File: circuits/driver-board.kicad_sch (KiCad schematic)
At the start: 74 parts, among them J1 Conn_01x18_Female, J2 USB4120-03-C_REVA, J3 Motor_Conn_01x04, J4 Screw_Terminals, J5 Conn_01x06_Female, Q1 SS8050-G, Q2 SS8050-G, SW1 RST_SW_Push, U1 CP2102N-Axx-xQFN24, U2 BA33DD0T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

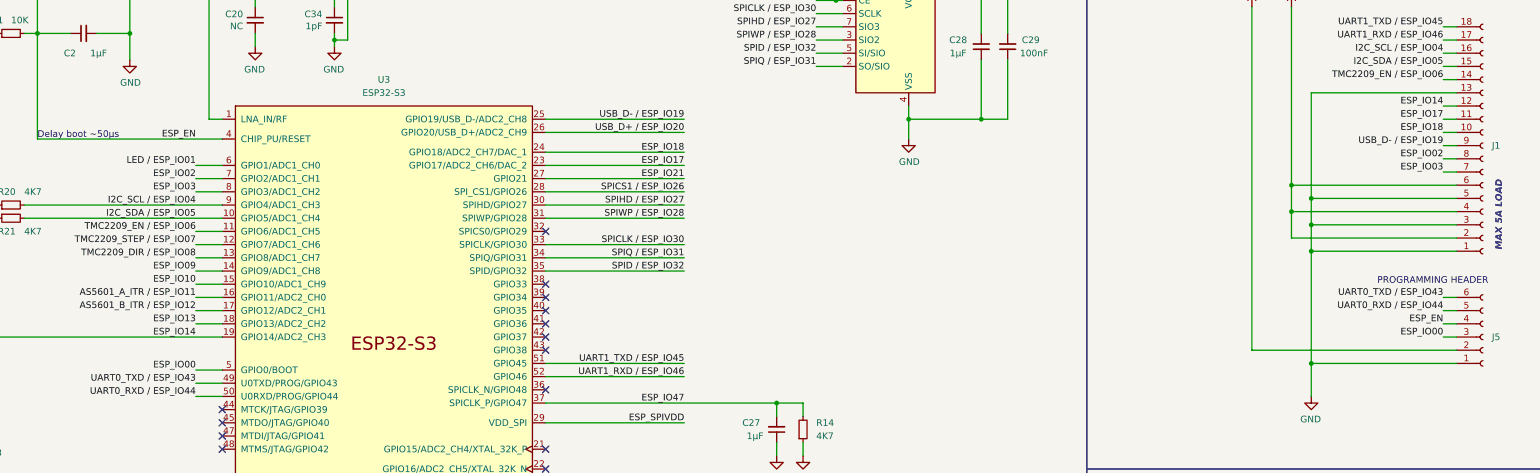
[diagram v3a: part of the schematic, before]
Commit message: another round of overall placement
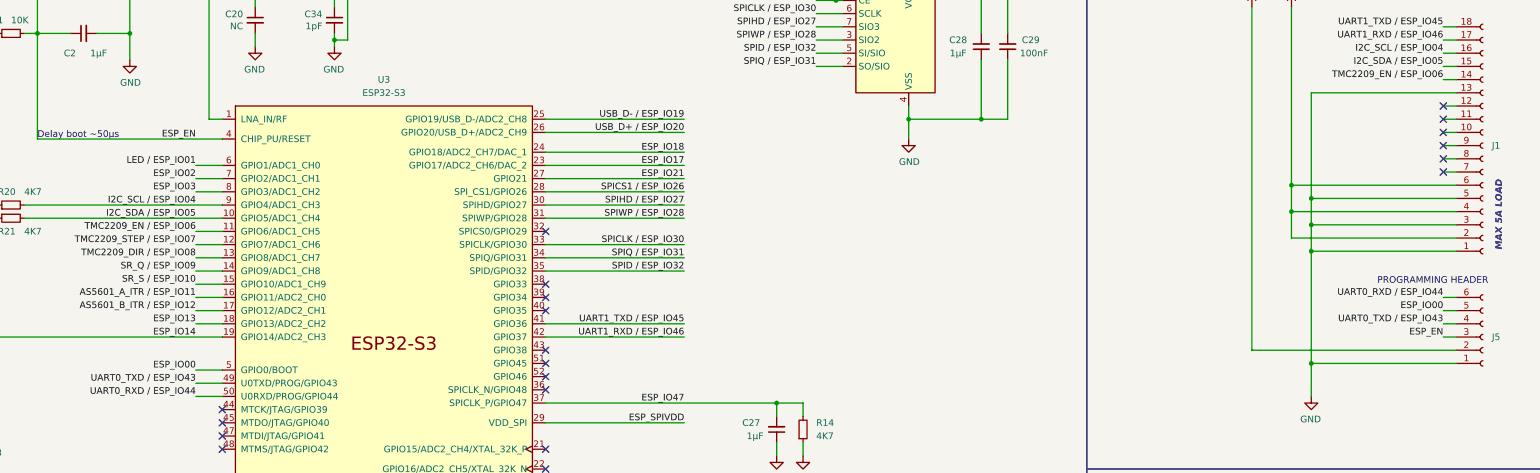
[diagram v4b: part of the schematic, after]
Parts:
- U8: footprint Package_SON:X2SON-8_1.4x1mm_P0.35mm -> Package_SO:TSSOP-8_3x3mm_P0.65mm
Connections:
- net ESP_IO09 is gone; now on net SR_Q / ESP_IO09: U3.14 (GPIO9/ADC1_CH8)
- net ESP_IO10 is gone; now on net SR_S / ESP_IO10: U3.15 (GPIO10/ADC1_CH9)
- net ESP_EN: now also J5.3 (Pin_3); no longer J5.4 (Pin_4)
- net ESP_IO00: now also J5.5 (Pin_5); no longer J5.3 (Pin_3)
- net ESP_IO02: no longer J1.8 (Pin_8)
- net ESP_IO03: no longer J1.7 (Pin_7)
- net ESP_IO14: no longer J1.12 (Pin_12)
- net ESP_IO17: no longer J1.11 (Pin_11)
- net ESP_IO18: no longer J1.10 (Pin_10)
- net UART0_RXD / ESP_IO44: now also J5.6 (Pin_6); no longer J5.5 (Pin_5)
- net UART0_TXD / ESP_IO43: now also J5.4 (Pin_4); no longer J5.6 (Pin_6)
- net UART1_RXD / ESP_IO46: now also U3.42 (GPIO37); no longer U3.52 (GPIO46)
- net UART1_TXD / ESP_IO45: now also U3.41 (GPIO36); no longer U3.51 (GPIO45)
- net USB_D- / ESP_IO19: no longer J1.9 (Pin_9)
- no-connect marks 48 -> 54
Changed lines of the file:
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@@
   (no_connect (at 69.85 63.5))
   (no_connect (at 64.77 246.38))
+  (no_connect (at 302.26 243.84))
   (no_connect (at 240.03 257.81))
   (no_connect (at 85.09 157.48))
+  (no_connect (at 474.98 199.39))
   (no_connect (at 240.03 252.73))
   (no_connect (at 54.61 157.48))
@@
   (no_connect (at 64.77 259.08))
   (no_connect (at 85.09 170.18))
+  (no_connect (at 474.98 196.85))
+  (no_connect (at 302.26 246.38))
   (no_connect (at 474.98 116.84))
   (no_connect (at 227.33 114.3))
@@
   (no_connect (at 74.93 132.08))
   (no_connect (at 227.33 68.58))
+  (no_connect (at 474.98 207.01))
   (no_connect (at 240.03 255.27))
-  (no_connect (at 302.26 238.76))
   (no_connect (at 227.33 71.12))
   (no_connect (at 54.61 172.72))
   (no_connect (at 64.77 264.16))
+  (no_connect (at 474.98 194.31))
+  (no_connect (at 474.98 201.93))
   (no_connect (at 302.26 231.14))
   (no_connect (at 302.26 233.68))
   (no_connect (at 64.77 256.54))
+  (no_connect (at 474.98 204.47))
   (no_connect (at 85.09 167.64))
-  (no_connect (at 302.26 236.22))
   (no_connect (at 240.03 260.35))
   (no_connect (at 302.26 248.92))
@@
     (stroke (width 0) (type default) (color 0 0 0 0))
   )
-  (wire (pts (xy 302.26 243.84) (xy 328.93 243.84))
+  (wire (pts (xy 302.26 236.22) (xy 328.93 236.22))
     (stroke (width 0) (type default) (color 0 0 0 0))
   )
@@
     (stroke (width 0) (type default) (color 0 0 0 0))
   )
-  (wire (pts (xy 302.26 246.38) (xy 328.93 246.38))
+  (wire (pts (xy 302.26 238.76) (xy 328.93 238.76))
     (stroke (width 0) (type default) (color 0 0 0 0))
   )
@@
     (effects (font (size 1.27 1.27)) (justify right bottom))
   )
-  (label "UART0_RXD {slash} ESP_IO44" (at 474.98 233.68 180)
+  (label "UART0_RXD {slash} ESP_IO44" (at 474.98 231.14 180)
     (effects (font (size 1.27 1.27)) (justify right bottom))
   )
@@
     (effects (font (size 1.27 1.27)) (justify right bottom))
   )
-  (label "ESP_IO00" (at 474.98 238.76 180)
+  (label "ESP_IO00" (at 474.98 233.68 180)
     (effects (font (size 1.27 1.27)) (justify right bottom))
   )
@@
     (effects (font (size 1.27 1.27)) (justify right bottom))
   )
-  (label "ESP_IO10" (at 234.95 228.6 180)
-    (effects (font (size 1.27 1.27)) (justify right bottom))
-  )
   (label "TMC2209_DIAG" (at 222.25 101.6 180)
     (effects (font (size 1.27 1.27)) (justify right bottom))
@@
     (effects (font (size 1.27 1.27)) (justify right bottom))
   )
-  (label "ESP_IO03" (at 474.98 207.01 180)
-    (effects (font (size 1.27 1.27)) (justify right bottom))
-  )
   (label "TMC2209_OB2" (at 281.94 95.25 180)
     (effects (font (size 1.27 1.27)) (justify right bottom))
@@
     (effects (font (size 1.27 1.27)) (justify right bottom))
   )
-  (label "UART1_RXD {slash} ESP_IO46" (at 328.93 246.38 180)
+  (label "UART1_RXD {slash} ESP_IO46" (at 328.93 238.76 180)
     (effects (font (size 1.27 1.27)) (justify right bottom))
   )
@@
     (effects (font (size 1.27 1.27)) (justify right bottom))
   )
-  (label "ESP_IO09" (at 234.95 226.06 180)
-    (effects (font (size 1.27 1.27)) (justify right bottom))
-  )
   (label "LED {slash} ESP_IO01" (at 234.95 205.74 180)
     (effects (font (size 1.27 1.27)) (justify right bottom))
@@
     (effects (font (size 1.27 1.27)) (justify right bottom))
   )
-  (label "UART0_TXD {slash} ESP_IO43" (at 474.98 231.14 180)
+  (label "UART0_TXD {slash} ESP_IO43" (at 474.98 236.22 180)
     (effects (font (size 1.27 1.27)) (justify right bottom))
   )
@@
     (effects (font (size 1.27 1.27)) (justify right bottom))
   )
+  (label "SR_Q {slash} ESP_IO09" (at 234.95 226.06 180)
+    (effects (font (size 1.27 1.27)) (justify right bottom))
+  )
   (label "ESP_IO21" (at 328.93 208.28 180)
     (effects (font (size 1.27 1.27)) (justify right bottom))
@@
     (effects (font (size 1.27 1.27)) (justify right bottom))
   )
-  (label "ESP_EN" (at 474.98 236.22 180)
+  (label "ESP_EN" (at 474.98 238.76 180)
     (effects (font (size 1.27 1.27)) (justify right bottom))
   )
@@
     (effects (font (size 1.27 1.27)) (justify left bottom))
   )
-  (label "ESP_IO17" (at 474.98 196.85 180)
-    (effects (font (size 1.27 1.27)) (justify right bottom))
-  )
   (label "ESP_IO14" (at 234.95 238.76 180)
     (effects (font (size 1.27 1.27)) (justify right bottom))
@@
     (effects (font (size 1.27 1.27)) (justify left bottom))
   )
-  (label "SPIWP {slash} ESP_IO28" (at 328.93 215.9 180)
+  (label "SR_S {slash} ESP_IO10" (at 234.95 228.6 180)
     (effects (font (size 1.27 1.27)) (justify right bottom))
   )
-  (label "ESP_IO14" (at 474.98 194.31 180)
+  (label "SPIWP {slash} ESP_IO28" (at 328.93 215.9 180)
     (effects (font (size 1.27 1.27)) (justify right bottom))
   )
@@
     (effects (font (size 1.27 1.27)) (justify right bottom))
   )
-  (label "ESP_IO18" (at 474.98 199.39 180)
-    (effects (font (size 1.27 1.27)) (justify right bottom))
-  )
   (label "UART1_RXD {slash} ESP_IO46" (at 474.98 181.61 180)
     (effects (font (size 1.27 1.27)) (justify right bottom))
@@
     (effects (font (size 1.27 1.27)) (justify right bottom))
   )
-  (label "USB_D- {slash} ESP_IO19" (at 474.98 201.93 180)
-    (effects (font (size 1.27 1.27)) (justify right bottom))
-  )
   (label "USB_D+" (at 107.95 60.96 0)
     (effects (font (size 1.27 1.27)) (justify left bottom))
@@
     (effects (font (size 1.27 1.27)) (justify right bottom))
   )
-  (label "ESP_IO02" (at 474.98 204.47 180)
-    (effects (font (size 1.27 1.27)) (justify right bottom))
-  )
   (label "UART1_TXD {slash} ESP_IO45" (at 207.01 73.66 180)
     (effects (font (size 1.27 1.27)) (justify right bottom))
   )
-  (label "UART1_TXD {slash} ESP_IO45" (at 328.93 243.84 180)
+  (label "UART1_TXD {slash} ESP_IO45" (at 328.93 236.22 180)
     (effects (font (size 1.27 1.27)) (justify right bottom))
   )
@@
       (effects (font (size 1.27 1.27)) hide)
     )
-    (property "Footprint" "Package_SON:X2SON-8_1.4x1mm_P0.35mm" (id 2) (at 372.11 129.54 0)
+    (property "Footprint" "Package_SO:TSSOP-8_3x3mm_P0.65mm" (id 2) (at 372.11 129.54 0)
       (effects (font (size 1.27 1.27)) hide)
     )
@@
     (property "Reference" "U8" (id 0) (at 373.38 114.3 0))
     (property "Value" "74LVC2G00" (id 1) (at 363.22 110.49 0))
-    (property "Footprint" "Package_SON:X2SON-8_1.4x1mm_P0.35mm" (id 2) (at 372.11 114.3 0)
+    (property "Footprint" "Package_SO:TSSOP-8_3x3mm_P0.65mm" (id 2) (at 372.11 114.3 0)
       (effects (font (size 1.27 1.27)) hide)
     )
@@
     )
     (path "/556ac974-9db3-4485-862d-ab386d9379e5"
-      (reference "U8") (unit 1) (value "74LVC2G00") (footprint "Package_SON:X2SON-8_1.4x1mm_P0.35mm")
+      (reference "U8") (unit 1) (value "74LVC2G00") (footprint "Package_SO:TSSOP-8_3x3mm_P0.65mm")
     )
     (path "/248c1e11-ccfb-48a8-8f7d-9b8a22293b8c"
-      (reference "U8") (unit 2) (value "74LVC2G00") (footprint "Package_SON:X2SON-8_1.4x1mm_P0.35mm")
+      (reference "U8") (unit 2) (value "74LVC2G00") (footprint "Package_SO:TSSOP-8_3x3mm_P0.65mm")
     )
     (path "/2eabefb1-a485-4f8d-a57b-22102eead219"

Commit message: first tracing
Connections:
- net I2C_SCL / ESP_IO04: now also J1.15 (Pin_15); no longer J1.16 (Pin_16)
- net I2C_SDA / ESP_IO05: now also J1.16 (Pin_16); no longer J1.15 (Pin_15)
- net TMC2209_STEP / ESP_IO15: now reaches U3.21 (GPIO15/ADC2_CH4/XTAL_32K_P)
- net TMC2209_STEP / ESP_IO15: now also U5.16 (STEP)
- net TMC2209_DIR / ESP_IO16: now reaches U3.22 (GPIO16/ADC2_CH5/XTAL_32K_N)
- net TMC2209_DIR / ESP_IO16: now also U5.19 (DIR)
- net ESP_IO18 renamed SR_Q / ESP_IO18
- net SR_Q / ESP_IO18: now also U8.5, U8.7
- net ESP_IO21 renamed SR_S / ESP_IO21
- net SR_S / ESP_IO21: now also R18.1, R2.2, U8.6
- removed net SR_Q / ESP_IO09: U3.14 (GPIO9/ADC1_CH8), U8.5, U8.7
- removed net SR_S / ESP_IO10: R18.1, R2.2, U3.15 (GPIO10/ADC1_CH9), U8.6
- net TMC2209_DIR / ESP_IO08: no longer names the net of U3.13 (GPIO8/ADC1_CH7)
- net TMC2209_DIR / ESP_IO08: no longer U5.19 (DIR)
- net TMC2209_STEP / ESP_IO07: no longer names the net of U3.12 (GPIO7/ADC1_CH6)
- net TMC2209_STEP / ESP_IO07: no longer U5.16 (STEP)
- new net ESP_IO09: U3.14 (GPIO9/ADC1_CH8)
- new net ESP_IO10: U3.15 (GPIO10/ADC1_CH9)
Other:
- moved on the sheet: J2, R5, R6

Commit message: first finished tracing; missing expboard connections and bom
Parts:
- removed R2: 20K, Resistor_SMD:R_0402_1005Metric, symbol Device:R_Small
- added C17: 100nF, Capacitor_SMD:C_0402_1005Metric, symbol Device:C_Small
- C5: value 1µF -> 10µF
- C7: value 10nF -> 1µF
- R20, R21: footprint Resistor_SMD:R_0201_0603Metric -> Resistor_SMD:R_0402_1005Metric
- R7: footprint Resistor_SMD:R_0402_1005Metric -> Resistor_SMD:R_0201_0603Metric
- U5: footprint Package_DFN_QFN:QFN-28-1EP_5x5mm_P0.5mm_EP3.35x3.35mm_ThermalVias -> trinamic-footprints:QFN28P
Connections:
- net ESP_IO09 is gone; now on net AS5601_A_ITR / ESP_IO09: U3.14 (GPIO9/ADC1_CH8)
- net ESP_IO10 is gone; now on net AS5601_B_ITR / ESP_IO10: U3.15 (GPIO10/ADC1_CH9)
- net +3V3: now also C17.2
- net GND: now also C17.1
- net I2C_SCL / ESP_IO04: now also J1.17 (Pin_17); no longer J1.15 (Pin_15)
- net I2C_SDA / ESP_IO05: now also J1.18 (Pin_18); no longer J1.16 (Pin_16)
- net TMC2209_EN / ESP_IO06: now also J1.16 (Pin_16); no longer J1.14 (Pin_14)
- net UART1_RXD / ESP_IO46: no longer J1.17 (Pin_17)
- net UART1_TXD / ESP_IO45: no longer J1.18 (Pin_18)
- net TMC2209_BRB: now reaches R13.2, U5.27 (BRB)
- net TMC2209_BRA: now reaches R12.2, U5.23 (BRA)
- net ANTENNA: now reaches AE1.1 (A), C34.1, L1.1
- net AS5601_A_ITR / ESP_IO11 renamed AS5601_A_ITR / ESP_IO09
- net AS5601_A_ITR / ESP_IO09: no longer U3.16 (GPIO11/ADC2_CH0)
- net AS5601_B_ITR / ESP_IO12 renamed AS5601_B_ITR / ESP_IO10
- net AS5601_B_ITR / ESP_IO10: no longer U3.17 (GPIO12/ADC2_CH1)
- net ESP_IO14 renamed VBUS_SENSE / ESP_IO14
- net LED / ESP_IO01 renamed ESP_IO01
- net ESP_IO01: no longer R4.1
- new net ESP_IO12: U3.17 (GPIO12/ADC2_CH1)
- new net LED / ESP_IO11: R4.1, U3.16 (GPIO11/ADC2_CH0)
- no-connect marks 54 -> 56
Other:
- note removed: "PULL TO BE DETERMINED"
- moved on the sheet: AE1, C25, C30, C31, C32, C33, C34, J3, R12, R13, R18

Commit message: updated groundplanes
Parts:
- removed R10, R8: 5K1, Resistor_SMD:R_0402_1005Metric, symbol Device:R_Small
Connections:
- net GND: now also J1.15 (Pin_15); no longer J1.13 (Pin_13)
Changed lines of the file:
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@@
   (junction (at 326.39 57.15) (diameter 0) (color 0 0 0 0)
   )
-  (junction (at 50.8 142.24) (diameter 0) (color 0 0 0 0)
-  )
   (junction (at 340.36 276.86) (diameter 0) (color 0 0 0 0)
   )
+  (junction (at 50.8 149.86) (diameter 0) (color 0 0 0 0)
+  )
   (junction (at 265.43 57.15) (diameter 0) (color 0 0 0 0)
   )
@@
   (junction (at 236.22 279.4) (diameter 0) (color 0 0 0 0)
   )
+  (junction (at 50.8 142.24) (diameter 0) (color 0 0 0 0)
+  )
   (junction (at 467.36 106.68) (diameter 0) (color 0 0 0 0)
   )
@@
   (junction (at 327.66 269.24) (diameter 0) (color 0 0 0 0)
   )
-  (junction (at 50.8 149.86) (diameter 0) (color 0 0 0 0)
-  )
   (junction (at 316.23 57.15) (diameter 0) (color 0 0 0 0)
   )
@@
   (junction (at 275.59 181.61) (diameter 0) (color 0 0 0 0)
   )
-  (junction (at 26.67 149.86) (diameter 0) (color 0 0 0 0)
-  )
   (junction (at 331.47 57.15) (diameter 0) (color 0 0 0 0)
   )
@@
   (no_connect (at 64.77 246.38))
   (no_connect (at 302.26 243.84))
+  (no_connect (at 474.98 191.77))
   (no_connect (at 240.03 257.81))
   (no_connect (at 85.09 157.48))
@@
   (no_connect (at 64.77 259.08))
   (no_connect (at 85.09 170.18))
-  (no_connect (at 474.98 186.69))
   (no_connect (at 474.98 196.85))
   (no_connect (at 302.26 246.38))
@@
     (stroke (width 0) (type default) (color 0 0 0 0))
   )
-  (wire (pts (xy 26.67 154.94) (xy 26.67 149.86))
-    (stroke (width 0) (type default) (color 0 0 0 0))
-  )
   (wire (pts (xy 467.36 106.68) (xy 467.36 109.22))
     (stroke (width 0) (type default) (color 0 0 0 0))
@@
     (stroke (width 0) (type default) (color 0 0 0 0))
   )
-  (wire (pts (xy 26.67 142.24) (xy 26.67 149.86))
-    (stroke (width 0) (type default) (color 0 0 0 0))
-  )
   (wire (pts (xy 354.33 173.99) (xy 358.14 173.99))
     (stroke (width 0) (type default) (color 0 0 0 0))
@@
     (stroke (width 0) (type default) (color 0 0 0 0))
   )
+  (wire (pts (xy 46.99 149.86) (xy 50.8 149.86))
+    (stroke (width 0) (type default) (color 0 0 0 0))
+  )
   (wire (pts (xy 199.39 93.98) (xy 214.63 93.98))
     (stroke (width 0) (type default) (color 0 0 0 0))
@@
     (stroke (width 0) (type default) (color 0 0 0 0))
   )
-  (wire (pts (xy 26.67 149.86) (xy 31.75 149.86))
-    (stroke (width 0) (type default) (color 0 0 0 0))
-  )
   (wire (pts (xy 386.08 162.56) (xy 391.16 162.56))
     (stroke (width 0) (type default) (color 0 0 0 0))
@@
     (stroke (width 0) (type default) (color 0 0 0 0))
   )
-  (wire (pts (xy 449.58 191.77) (xy 449.58 212.09))
+  (wire (pts (xy 449.58 186.69) (xy 449.58 212.09))
     (stroke (width 0) (type default) (color 0 0 0 0))
   )
@@
     (stroke (width 0) (type default) (color 0 0 0 0))
   )
-  (wire (pts (xy 36.83 149.86) (xy 50.8 149.86))
-    (stroke (width 0) (type default) (color 0 0 0 0))
-  )
   (wire (pts (xy 275.59 181.61) (xy 275.59 182.88))
     (stroke (width 0) (type default) (color 0 0 0 0))
@@
     (stroke (width 0) (type default) (color 0 0 0 0))
   )
+  (wire (pts (xy 46.99 142.24) (xy 50.8 142.24))
+    (stroke (width 0) (type default) (color 0 0 0 0))
+  )
   (wire (pts (xy 234.95 208.28) (xy 240.03 208.28))
     (stroke (width 0) (type default) (color 0 0 0 0))
@@
     (stroke (width 0) (type default) (color 0 0 0 0))
   )
-  (wire (pts (xy 31.75 142.24) (xy 26.67 142.24))
-    (stroke (width 0) (type default) (color 0 0 0 0))
-  )
   (wire (pts (xy 25.4 88.9) (xy 25.4 93.98))
     (stroke (width 0) (type default) (color 0 0 0 0))
@@
     (stroke (width 0) (type default) (color 0 0 0 0))
   )
-  (wire (pts (xy 474.98 186.69) (xy 477.52 186.69))
+  (wire (pts (xy 449.58 186.69) (xy 477.52 186.69))
     (stroke (width 0) (type default) (color 0 0 0 0))
   )
@@
     (stroke (width 0) (type default) (color 0 0 0 0))
   )
-  (wire (pts (xy 449.58 191.77) (xy 477.52 191.77))
-    (stroke (width 0) (type default) (color 0 0 0 0))
-  )
   (wire (pts (xy 316.23 57.15) (xy 316.23 59.69))
     (stroke (width 0) (type default) (color 0 0 0 0))
@@
     (stroke (width 0) (type default) (color 0 0 0 0))
   )
-  (wire (pts (xy 36.83 142.24) (xy 50.8 142.24))
-    (stroke (width 0) (type default) (color 0 0 0 0))
-  )
   (wire (pts (xy 379.73 113.03) (xy 383.54 113.03))
     (stroke (width 0) (type default) (color 0 0 0 0))
@@
     (stroke (width 0) (type default) (color 0 0 0 0))
   )
+  (wire (pts (xy 474.98 191.77) (xy 477.52 191.77))
+    (stroke (width 0) (type default) (color 0 0 0 0))
+  )
   (wire (pts (xy 121.92 78.74) (xy 121.92 82.55))
     (stroke (width 0) (type default) (color 0 0 0 0))
@@
     (effects (font (size 1.27 1.27)) (justify right bottom))
   )
-  (label "USB_CC1" (at 49.53 142.24 180)
+  (label "USB_CC1" (at 46.99 142.24 180)
     (effects (font (size 1.27 1.27)) (justify right bottom))
   )
@@
     (effects (font (size 1.27 1.27)) (justify left bottom))
   )
-  (label "USB_CC2" (at 49.53 149.86 180)
+  (label "USB_CC2" (at 46.99 149.86 180)
     (effects (font (size 1.27 1.27)) (justify right bottom))
   )
@@
     (pin "9")
   )
-  (symbol (lib_id "power:GND") (at 26.67 154.94 0) (unit 1)
-    (in_bom yes) (on_board yes)
-    (property "Reference" "#PWR041" (id 0) (at 26.67 161.29 0)
-      (effects (font (size 1.27 1.27)) hide)
-    )
-    (property "Value" "GND" (id 1) (at 26.797 159.3342 0))
-    (property "Footprint" "" (id 2) (at 26.67 154.94 0)
-      (effects (font (size 1.27 1.27)) hide)
-    )
-    (property "Datasheet" "" (id 3) (at 26.67 154.94 0)
-      (effects (font (size 1.27 1.27)) hide)
-    )
-    (pin "1")
-  )
   (symbol (lib_id "Device:Antenna_Shield") (at 275.59 165.1 0) (unit 1)
     (in_bom yes) (on_board yes)
@@
     (pin "1")
   )
-  (symbol (lib_id "Device:R_Small") (at 34.29 142.24 270) (mirror x) (unit 1)
-    (in_bom yes) (on_board yes)
-    (property "Reference" "R8" (id 0) (at 30.48 139.7 90)
-      (effects (font (size 1.27 1.27)) (justify left))
-    )
-    (property "Value" "5K1" (id 1) (at 34.29 139.7 90)
-      (effects (font (size 1.27 1.27)) (justify left))
-    )
-    (property "Footprint" "Resistor_SMD:R_0402_1005Metric" (id 2) (at 34.29 142.24 0)
-      (effects (font (size 1.27 1.27)) hide)
-    )
-    (property "Datasheet" "~" (id 3) (at 34.29 142.24 0)
-      (effects (font (size 1.27 1.27)) hide)
-    )
-    (pin "1")
-    (pin "2")
-  )
   (symbol (lib_id "Device:C_Small") (at 386.08 182.88 180) (unit 1)
     (in_bom yes) (on_board yes)
@@
     (pin "2")
   )
-  (symbol (lib_id "Device:R_Small") (at 34.29 149.86 270) (mirror x) (unit 1)
-    (in_bom yes) (on_board yes)
-    (property "Reference" "R10" (id 0) (at 30.48 147.32 90)
-      (effects (font (size 1.27 1.27)) (justify left))
-    )
-    (property "Value" "5K1" (id 1) (at 34.29 147.32 90)
-      (effects (font (size 1.27 1.27)) (justify left))
-    )
-    (property "Footprint" "Resistor_SMD:R_0402_1005Metric" (id 2) (at 34.29 149.86 0)
-      (effects (font (size 1.27 1.27)) hide)
-    )
-    (property "Datasheet" "~" (id 3) (at 34.29 149.86 0)
-      (effects (font (size 1.27 1.27)) hide)
-    )
-    (pin "1")
-    (pin "2")
-  )
   (symbol (lib_id "Device:R_Small") (at 199.39 180.34 90) (unit 1)
     (in_bom yes) (on_board yes)
@@
       (reference "#PWR040") (unit 1) (value "GND") (footprint "")
     )
-    (path "/22dc10af-bdd2-4608-9314-19c1d003d651"
-      (reference "#PWR041") (unit 1) (value "GND") (footprint "")
-    )
     (path "/fdc998f3-f202-4ff3-81c3-f8d6718ec0c3"
       (reference "#PWR042") (unit 1) (value "+3V3") (footprint "")
@@
       (reference "R7") (unit 1) (value "20K") (footprint "Resistor_SMD:R_0201_0603Metric")
     )
-    (path "/429cd460-d727-47f7-9f64-52e357f9e6cc"
-      (reference "R8") (unit 1) (value "5K1") (footprint "Resistor_SMD:R_0402_1005Metric")
-    )
     (path "/923bf67d-dc0f-41ed-a99d-350ba970709a"
       (reference "R9") (unit 1) (value "100K") (footprint "Resistor_SMD:R_0402_1005Metric")
     )
-    (path "/ed158ec7-dd4c-440f-8f52-e5ea7718d07c"
-      (reference "R10") (unit 1) (value "5K1") (footprint "Resistor_SMD:R_0402_1005Metric")
-    )
     (path "/00000000-0000-0000-0000-0000609c62c6"
